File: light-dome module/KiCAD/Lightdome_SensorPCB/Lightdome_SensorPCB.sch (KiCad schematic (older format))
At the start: 6 parts, among them J1 Conn_01x04, U1 VEML6070, U2 VEML7700-TT, U3 P82B715D

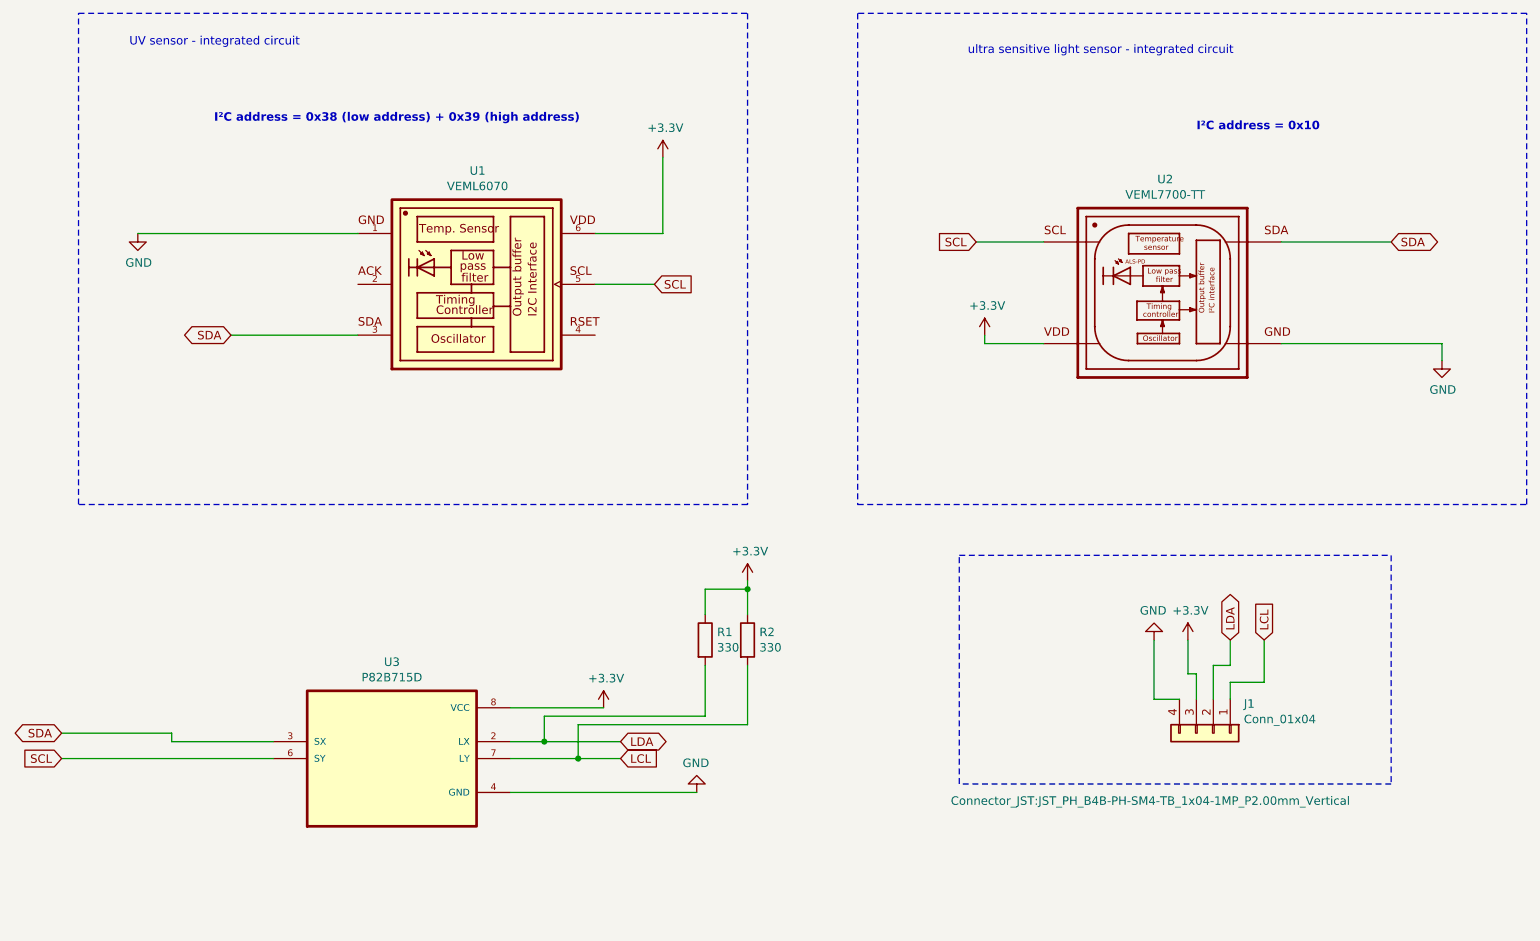
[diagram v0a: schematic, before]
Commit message: changes in light module PCB
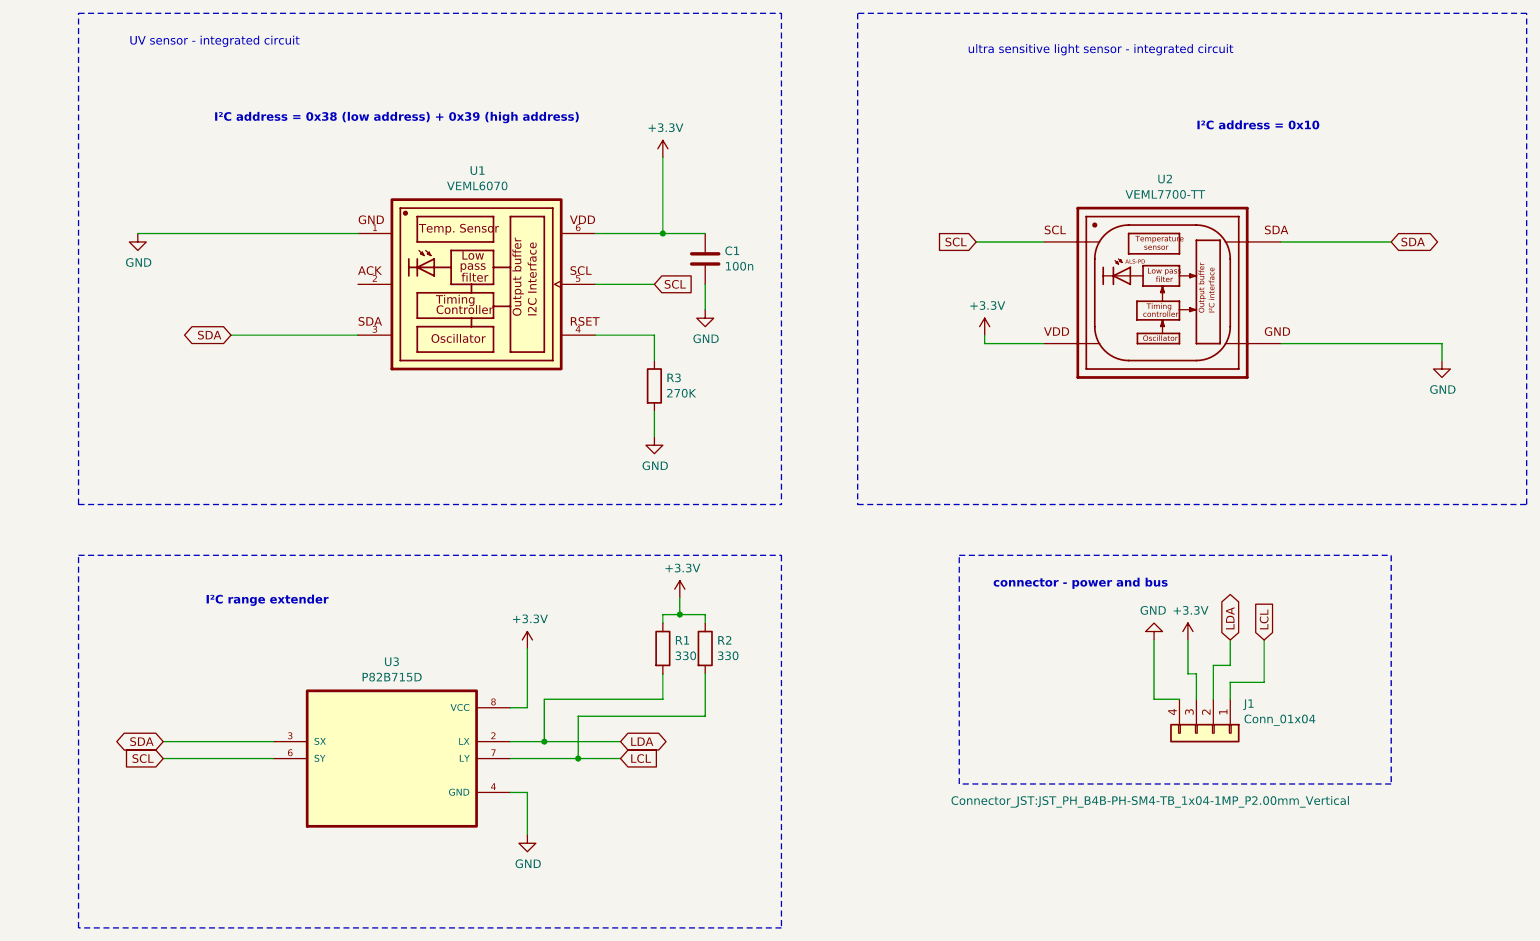
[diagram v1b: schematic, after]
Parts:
- added C1: 100n, Capacitor_SMD:C_0603_1608Metric_Pad1.05x0.95mm_HandSolder, symbol Device:C
- added R3: 270K, Resistor_SMD:R_0603_1608Metric_Pad1.05x0.95mm_HandSolder, symbol Device:R
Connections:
- net +3V3: now also C1.1
- net GND: now also C1.2, R3.2
- net at U1.4: now also R3.1
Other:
- note added: "I²C range extender"
- note added: "connector - power and bus"
- moved on the sheet: R1, R2
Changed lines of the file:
@@
 Text GLabel 8550 5050 1    50   Input ~ 0
 LCL
+Wire Wire Line
+	7900 5050 7900 5400
+Wire Wire Line
+	7900 5400 8050 5400
+Wire Wire Line
+	8100 5050 8100 5250
+Wire Wire Line
+	8100 5250 8150 5250
+Wire Wire Line
+	8150 5250 8150 5400
+Wire Wire Line
+	8350 5050 8350 5200
+Wire Wire Line
+	8350 5200 8250 5200
+Wire Wire Line
+	8250 5200 8250 5400
+Wire Wire Line
+	8550 5050 8550 5300
+Wire Wire Line
+	8550 5300 8350 5300
+Wire Wire Line
+	8350 5300 8350 5400
+Wire Wire Line
+	9300 2700 8650 2700
+Wire Wire Line
+	7250 2700 6850 2700
+Wire Wire Line
+	4950 2950 4600 2950
+Wire Wire Line
+	3200 3250 2450 3250
+Wire Notes Line
+	6150 4250 10100 4250
+Wire Notes Line
+	10100 4250 10100 1350
+Wire Notes Line
+	10100 1350 6150 1350
+Wire Notes Line
+	6150 1350 6150 4250
+Wire Notes Line
+	5700 1350 5700 4250
+Wire Notes Line
+	1550 4250 1550 1350
+Wire Notes Line
+	6750 4550 9300 4550
+Wire Notes Line
+	9300 4550 9300 5900
+Wire Notes Line
+	9300 5900 6750 5900
+Wire Notes Line
+	6750 5900 6750 4550
+Text Notes 1850 1550 0    50   ~ 0
+UV sensor - integrated circuit
+Text Notes 6800 1600 0    50   ~ 0
+ultra sensitive light sensor - integrated circuit
+Text Notes 8150 2050 0    50   ~ 10
+I²C address = 0x10
+Text Notes 2350 2000 0    50   ~ 10
+I²C address = 0x38 (low address) + 0x39 (high address)
+$Comp
+L P82B715D:P82B715D U3
+U 1 1 5FBBA2D9
+P 3400 5750
+F 0 "U3" H 3400 6320 50  0000 C CNN
+F 1 "P82B715D" H 3400 6229 50  0000 C CNN
+F 2 "SOIC127P599X175-8N" H 3400 5750 50  0001 L BNN
+F 3 "" H 3400 5750 50  0001 L BNN
+	1    3400 5750
+	1    0    0    -1
+$EndComp
+Text GLabel 4750 5650 2    50   BiDi ~ 0
+LDA
+Text GLabel 4750 5750 2    50   Input ~ 0
+LCL
+Wire Wire Line
+	4100 5650 4300 5650
+Wire Wire Line
+	4100 5750 4500 5750
+Text GLabel 2050 5750 0    50   Input ~ 0
+SCL
+Text GLabel 2050 5650 0    50   BiDi ~ 0
+SDA
+$Comp
+L power:+3.3V #PWR07
+U 1 1 5FBC4EE9
+P 4200 5100
+F 0 "#PWR07" H 4200 4950 50  0001 C CNN
+F 1 "+3.3V" H 4215 5273 50  0000 C CNN
+F 2 "" H 4200 5100 50  0001 C CNN
+F 3 "" H 4200 5100 50  0001 C CNN
+	1    4200 5100
+	1    0    0    -1
+$EndComp
+$Comp
+L power:GND #PWR08
+U 1 1 5FBC60FC
+P 4200 6200
+F 0 "#PWR08" H 4200 5950 50  0001 C CNN
+F 1 "GND" H 4205 6027 50  0000 C CNN
+F 2 "" H 4200 6200 50  0001 C CNN
+F 3 "" H 4200 6200 50  0001 C CNN
+	1    4200 6200
+	1    0    0    -1
+$EndComp
+$Comp
+L Device:R R1
+U 1 1 5FBD0962
+P 5000 5100
+F 0 "R1" H 5070 5146 50  0000 L CNN
+F 1 "330" H 5070 5055 50  0000 L CNN
+F 2 "Resistor_SMD:R_1206_3216Metric_Pad1.42x1.75mm_HandSolder" V 4930 5100 50  0001 C CNN
+F 3 "~" H 5000 5100 50  0001 C CNN
+	1    5000 5100
+	1    0    0    -1
+$EndComp
+Connection ~ 4300 5650
+Wire Wire Line
+	4300 5650 4750 5650
+Connection ~ 4500 5750
+Wire Wire Line
+	4500 5750 4750 5750
+$Comp
+L power:+3.3V #PWR09
+U 1 1 5FBD26E4
+P 5100 4800
+F 0 "#PWR09" H 5100 4650 50  0001 C CNN
+F 1 "+3.3V" H 5115 4973 50  0000 C CNN
+F 2 "" H 5100 4800 50  0001 C CNN
+F 3 "" H 5100 4800 50  0001 C CNN
+	1    5100 4800
+	1    0    0    -1
+$EndComp
 $Comp
 L Connector_Generic:Conn_01x04 J1
@@
 	0    1    1    0
 $EndComp
-Wire Wire Line
-	7900 5050 7900 5400
-Wire Wire Line
-	7900 5400 8050 5400
-Wire Wire Line
-	8100 5050 8100 5250
-Wire Wire Line
-	8100 5250 8150 5250
-Wire Wire Line
-	8150 5250 8150 5400
-Wire Wire Line
-	8350 5050 8350 5200
-Wire Wire Line
-	8350 5200 8250 5200
-Wire Wire Line
-	8250 5200 8250 5400
-Wire Wire Line
-	8550 5050 8550 5300
-Wire Wire Line
-	8550 5300 8350 5300
-Wire Wire Line
-	8350 5300 8350 5400
-Wire Wire Line
-	9300 2700 8650 2700
-Wire Wire Line
-	7250 2700 6850 2700
-Wire Wire Line
-	4950 2950 4600 2950
-Wire Wire Line
-	3200 3250 2450 3250
-Wire Notes Line
-	6150 4250 10100 4250
-Wire Notes Line
-	10100 4250 10100 1350
-Wire Notes Line
-	10100 1350 6150 1350
-Wire Notes Line
-	6150 1350 6150 4250
-Wire Notes Line
-	5500 1350 5500 4250
-Wire Notes Line
-	5500 4250 1550 4250
-Wire Notes Line
-	1550 4250 1550 1350
-Wire Notes Line
-	1550 1350 5500 1350
-Wire Notes Line
-	6750 4550 9300 4550
-Wire Notes Line
-	9300 4550 9300 5900
-Wire Notes Line
-	9300 5900 6750 5900
-Wire Notes Line
-	6750 5900 6750 4550
-Text Notes 1850 1550 0    50   ~ 0
-UV sensor - integrated circuit
-Text Notes 6800 1600 0    50   ~ 0
-ultra sensitive light sensor - integrated circuit
-Text Notes 8150 2050 0    50   ~ 10
-I²C address = 0x10
-Text Notes 2350 2000 0    50   ~ 10
-I²C address = 0x38 (low address) + 0x39 (high address)
-$Comp
-L P82B715D:P82B715D U3
-U 1 1 5FBBA2D9
-P 3400 5750
-F 0 "U3" H 3400 6320 50  0000 C CNN
-F 1 "P82B715D" H 3400 6229 50  0000 C CNN
-F 2 "SOIC127P599X175-8N" H 3400 5750 50  0001 L BNN
-F 3 "" H 3400 5750 50  0001 L BNN
-	1    3400 5750
-	1    0    0    -1
-$EndComp
-Text GLabel 4750 5650 2    50   BiDi ~ 0
-LDA
-Text GLabel 4750 5750 2    50   Input ~ 0
-LCL
-Wire Wire Line
-	4100 5650 4300 5650
-Wire Wire Line
-	4100 5750 4500 5750
-Text GLabel 1450 5750 0    50   Input ~ 0
-SCL
-Text GLabel 1450 5600 0    50   BiDi ~ 0
-SDA
-Wire Wire Line
-	2700 5650 2100 5650
-Wire Wire Line
-	2100 5650 2100 5600
-Wire Wire Line
-	2100 5600 1450 5600
-Wire Wire Line
-	2700 5750 1450 5750
-$Comp
-L power:+3.3V #PWR07
-U 1 1 5FBC4EE9
-P 4650 5450
-F 0 "#PWR07" H 4650 5300 50  0001 C CNN
-F 1 "+3.3V" H 4665 5623 50  0000 C CNN
-F 2 "" H 4650 5450 50  0001 C CNN
-F 3 "" H 4650 5450 50  0001 C CNN
-	1    4650 5450
-	1    0    0    -1
-$EndComp
-Wire Wire Line
-	4650 5450 4100 5450
-$Comp
-L power:GND #PWR08
-U 1 1 5FBC60FC
-P 5200 5950
-F 0 "#PWR08" H 5200 5700 50  0001 C CNN
-F 1 "GND" H 5205 5777 50  0000 C CNN
-F 2 "" H 5200 5950 50  0001 C CNN
-F 3 "" H 5200 5950 50  0001 C CNN
-	1    5200 5950
-	-1   0    0    1
-$EndComp
-Wire Wire Line
-	5200 5950 4100 5950
-$Comp
-L Device:R R1
-U 1 1 5FBD0962
-P 5250 5050
-F 0 "R1" H 5320 5096 50  0000 L CNN
-F 1 "330" H 5320 5005 50  0000 L CNN
-F 2 "Resistor_SMD:R_1206_3216Metric_Pad1.42x1.75mm_HandSolder" V 5180 5050 50  0001 C CNN
-F 3 "~" H 5250 5050 50  0001 C CNN
-	1    5250 5050
-	1    0    0    -1
-$EndComp
 $Comp
 L Device:R R2
 U 1 1 5FBD0F46
-P 5500 5050
-F 0 "R2" H 5570 5096 50  0000 L CNN
-F 1 "330" H 5570 5005 50  0000 L CNN
-F 2 "Resistor_SMD:R_1206_3216Metric_Pad1.42x1.75mm_HandSolder" V 5430 5050 50  0001 C CNN
-F 3 "~" H 5500 5050 50  0001 C CNN
-	1    5500 5050
-	1    0    0    -1
-$EndComp
-Wire Wire Line
-	5250 5200 5250 5500
-Wire Wire Line
-	5250 5500 4300 5500
-Wire Wire Line
-	4300 5500 4300 5650
-Connection ~ 4300 5650
-Wire Wire Line
-	4300 5650 4750 5650
-Wire Wire Line
-	5500 5200 5500 5550
-Wire Wire Line
-	5500 5550 4500 5550
-Wire Wire Line
-	4500 5550 4500 5750
-Connection ~ 4500 5750
-Wire Wire Line
-	4500 5750 4750 5750
-$Comp
-L power:+3.3V #PWR09
-U 1 1 5FBD26E4
-P 5500 4700
-F 0 "#PWR09" H 5500 4550 50  0001 C CNN
-F 1 "+3.3V" H 5515 4873 50  0000 C CNN
-F 2 "" H 5500 4700 50  0001 C CNN
-F 3 "" H 5500 4700 50  0001 C CNN
-	1    5500 4700
-	1    0    0    -1
-$EndComp
-Wire Wire Line
-	5500 4700 5500 4750
-Wire Wire Line
-	5250 4900 5250 4750
-Wire Wire Line
-	5250 4750 5500 4750
-Connection ~ 5500 4750
-Wire Wire Line
-	5500 4750 5500 4900
+P 5250 5100
+F 0 "R2" H 5320 5146 50  0000 L CNN
+F 1 "330" H 5320 5055 50  0000 L CNN
+F 2 "Resistor_SMD:R_1206_3216Metric_Pad1.42x1.75mm_HandSolder" V 5180 5100 50  0001 C CNN
+F 3 "~" H 5250 5100 50  0001 C CNN
+	1    5250 5100
+	1    0    0    -1
+$EndComp
+$Comp
+L Device:R R3
+U 1 1 5FBF76AF
+P 4950 3550
+F 0 "R3" H 5020 3596 50  0000 L CNN
+F 1 "270K" H 5020 3505 50  0000 L CNN
+F 2 "Resistor_SMD:R_0603_1608Metric_Pad1.05x0.95mm_HandSolder" V 4880 3550 50  0001 C CNN
+F 3 "~" H 4950 3550 50  0001 C CNN
+	1    4950 3550
+	1    0    0    -1
+$EndComp
+$Comp
+L power:GND #PWR010
+U 1 1 5FBF88F3
+P 4950 3850
+F 0 "#PWR010" H 4950 3600 50  0001 C CNN
+F 1 "GND" H 4955 3677 50  0000 C CNN
+F 2 "" H 4950 3850 50  0001 C CNN
+F 3 "" H 4950 3850 50  0001 C CNN
+	1    4950 3850
+	1    0    0    -1
+$EndComp
+Wire Wire Line
+	4600 3250 4950 3250
+Wire Wire Line
+	4950 3250 4950 3400
+Wire Wire Line
+	4950 3700 4950 3850
+$Comp
+L Device:C C1
+U 1 1 5FBFBD63
+P 5250 2800
+F 0 "C1" H 5365 2846 50  0000 L CNN
+F 1 "100n" H 5365 2755 50  0000 L CNN
+F 2 "Capacitor_SMD:C_0603_1608Metric_Pad1.05x0.95mm_HandSolder" H 5288 2650 50  0001 C CNN
+F 3 "~" H 5250 2800 50  0001 C CNN
+	1    5250 2800
+	1    0    0    -1
+$EndComp
+$Comp
+L power:GND #PWR011
+U 1 1 5FBFCA41
+P 5250 3100
+F 0 "#PWR011" H 5250 2850 50  0001 C CNN
+F 1 "GND" H 5255 2927 50  0000 C CNN
+F 2 "" H 5250 3100 50  0001 C CNN
+F 3 "" H 5250 3100 50  0001 C CNN
+	1    5250 3100
+	1    0    0    -1
+$EndComp
+Wire Wire Line
+	5250 2950 5250 3100
+Wire Wire Line
+	5250 2650 5000 2650
+Connection ~ 5000 2650
+Wire Notes Line
+	1550 1350 5700 1350
+Wire Notes Line
+	1550 4250 5700 4250
+Wire Wire Line
+	2700 5650 2050 5650
+Wire Wire Line
+	2050 5750 2700 5750
+Wire Notes Line
+	1550 4550 5700 4550
+Wire Notes Line
+	5700 4550 5700 6750
+Wire Notes Line
+	5700 6750 1550 6750
+Wire Notes Line
+	1550 6750 1550 4550
+Wire Wire Line
+	4200 5100 4200 5450
+Wire Wire Line
+	4200 5450 4100 5450
+Wire Wire Line
+	4100 5950 4200 5950
+Wire Wire Line
+	4200 5950 4200 6200
+Wire Wire Line
+	4500 5500 5250 5500
+Wire Wire Line
+	4500 5500 4500 5750
+Wire Wire Line
+	5250 5500 5250 5250
+Wire Wire Line
+	5000 5250 5000 5400
+Wire Wire Line
+	5000 5400 4300 5400
+Wire Wire Line
+	4300 5400 4300 5650
+Wire Wire Line
+	5000 4950 5000 4900
+Wire Wire Line
+	5000 4900 5100 4900
+Wire Wire Line
+	5250 4900 5250 4950
+Wire Wire Line
+	5100 4800 5100 4900
+Connection ~ 5100 4900
+Wire Wire Line
+	5100 4900 5250 4900
+Text Notes 2300 4850 0    50   ~ 10
+I²C range extender
+Text Notes 6950 4750 0    50   ~ 10
+connector - power and bus
 $EndSCHEMATC
